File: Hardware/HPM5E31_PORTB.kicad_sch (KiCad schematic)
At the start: 1 part, among them U1 HPM5E31IGN1

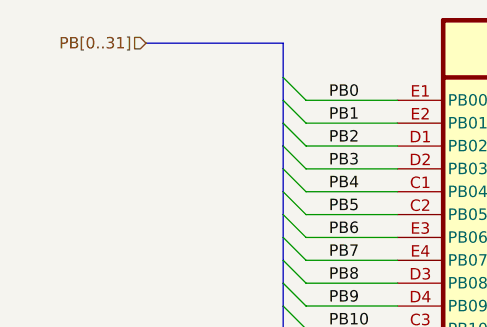
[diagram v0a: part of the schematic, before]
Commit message: 新增ESC IO引出，ESC CTR LED，EUI接口
编码器接口电源输出加保险，SPI加ESD
PY32ADC外部接口加ESD
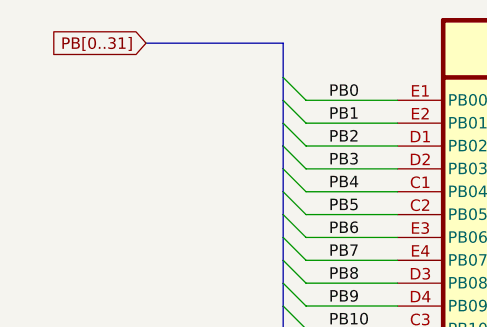
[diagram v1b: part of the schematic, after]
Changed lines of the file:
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@@
 		)
 	)
-	(hierarchical_label "PB[0..31]"
+	(global_label "PB[0..31]"
 		(shape input)
 		(at 58.42 67.31 180)
+		(fields_autoplaced yes)
 		(effects
 			(font
@@
 			(justify right)
 		)
+		(property "Intersheetrefs" "${INTERSHEET_REFS}"
+			(at 46.3633 67.31 0)
+			(effects
+				(font
+					(size 1.27 1.27)
+				)
+				(justify right)
+				(hide yes)
+			)
+		)
 	)

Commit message: 拉线
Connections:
- net PB0: now also U1.M2 (DCDC_IN); no longer U1.E1 (PB00/MCAN0.TXD/ESC0.P0_RXDV/PWM0.P0/TRGM.P00/ETH0.RXDV/QEO1.A)
- net PB1: no longer U1.E2 (PB01/MCAN0.RXD/ESC0.P0_RXD0/PWM0.P1/TRGM.P01/ETH0.RXD0/QEO1.B)
- net PB10: no longer U1.C3 (PB10/MCAN2.STBY/ESC0.P0_TXD3/PWM1.P2/TRGM.P10/ETH0.TXD3)
- net PB11: no longer U1.C4 (PB11/ESC0.P0_TXEN/PWM1.P3/TRGM.P11/ETH0.TXEN)
- net PB2: no longer U1.D1 (PB02/I2C2.SCL/MCAN0.STBY/ESC0.P0_RXD1/PWM0.P2/TRGM.P02/ETH0.RXD1/QEI0.H1/QEO1.Z)
- net PB24: no longer U1.A2 (PB24/ESC0.CTR4/XPI0.CA_CS1/SDM0.CLK3/ETH0.EVTI0/ESC0.EVTI0)
- net PB25: now also U1.J9 (VANA); no longer U1.B1 (PB25/ESC0.CTR5/XPI0.CA_DQS/SDM0.DAT3/ETH0.EVTO0/ESC0.EVTO0)
- net PB26: no longer U1.A3 (PB26/ESC0.CTR6/XPI0.CA_D2/QEI1.H1/SDM0.CLK2/ETH0.EVTI1/EUI1.CK/ESC0.EVTI1)
- net PB27: no longer U1.B2 (PB27/ESC0.CTR7/XPI0.CA_D0/QEI1.F/SDM0.DAT2/EUI1.SH)
- net PB28: now also U1.H8 (VSSA); no longer U1.A4 (PB28/ESC0.CTR8/XPI0.CA_D1/QEI1.H0/SDM0.CLK1/EUI1.DI)
- net PB29: no longer U1.B3 (PB29/XPI0.CA_SCLK/QEI1.Z/SDM0.DAT1/ETH0.EVTO1/EUI1.DO/ESC0.EVTO1)
- net PB3: now also U1.N2 (DCDC_LP); no longer U1.D2 (PB03/I2C2.SDA/MCAN1.STBY/ESC0.P0_RXD2/PWM0.P3/TRGM.P03/ETH0.RXD2/QEI0.F)
- net PB30: no longer U1.A5 (PB30/ESC0.CTR7/XPI0.CA_CS0/QEI1.A/SDM0.CLK0)
- net PB31: no longer U1.B4 (PB31/ESC0.CTR8/XPI0.CA_D3/QEI1.B/SDM0.DAT0)
- net PB4: now also U1.P3 (DCDC_LP); no longer U1.C1 (PB04/MCAN1.RXD/ESC0.P0_RXD3/PWM0.P4/TRGM.P04/ETH0.RXD3/QEI0.H0)
- net PB5: no longer U1.C2 (PB05/MCAN1.TXD/ESC0.P0_RXCK/PWM0.P5/TRGM.P05/ETH0.RXCK/QEI0.Z/QEO0.Z)
- net PB6: no longer U1.E3 (PB06/I2C3.SDA/ESC0.P0_TXCK/PWM0.P6/TRGM.P06/ETH0.TXCK/QEI0.B/QEO0.B)
- net PB7: no longer U1.E4 (PB07/I2C3.SCL/ESC0.P0_TXD0/PWM0.P7/TRGM.P07/ETH0.TXD0/QEI0.A/QEO0.A)
- net PB8: no longer U1.D3 (PB08/I2C0.SCL/MCAN2.TXD/ESC0.P0_TXD1/PWM1.P0/TRGM.P08/ETH0.TXD1)
- net PB9: no longer U1.D4 (PB09/I2C0.SDA/MCAN2.RXD/ESC0.P0_TXD2/PWM1.P1/TRGM.P09/ETH0.TXD2)
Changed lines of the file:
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@@
 		(lib_id "HPM5E00_Library:HPM5E31IGN1")
 		(at 91.44 64.77 0)
-		(unit 5)
+		(unit 1)
 		(exclude_from_sim no)
 		(in_bom yes)
@@
 		(pin "L6"
 		)
-		(instances
-			(project "HPM5E31_ECatDualFOC"
-				(path "/a07e9810-3899-4327-ba8f-f24142a7c70e/b9a8d5a3-7d25-4818-87f6-adc719379948/aa8aabb3-6958-433e-9267-bd903eafdb8f"
-					(reference "U1")
-					(unit 5)
-				)
-			)
-		)
 	)

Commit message: 修存档拉线
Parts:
- renumbered U1 to U3
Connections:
- net PB0: now also U3.E1 (PB00/MCAN0.TXD/ESC0.P0_RXDV/PWM0.P0/TRGM.P00/ETH0.RXDV/QEO1.A); no longer U3.M2 (DCDC_IN)
- net PB1: now also U3.E2 (PB01/MCAN0.RXD/ESC0.P0_RXD0/PWM0.P1/TRGM.P01/ETH0.RXD0/QEO1.B)
- net PB10: now also U3.C3 (PB10/MCAN2.STBY/ESC0.P0_TXD3/PWM1.P2/TRGM.P10/ETH0.TXD3)
- net PB11: now also U3.C4 (PB11/ESC0.P0_TXEN/PWM1.P3/TRGM.P11/ETH0.TXEN)
- net PB2: now also U3.D1 (PB02/I2C2.SCL/MCAN0.STBY/ESC0.P0_RXD1/PWM0.P2/TRGM.P02/ETH0.RXD1/QEI0.H1/QEO1.Z)
- net PB24: now also U3.A2 (PB24/ESC0.CTR4/XPI0.CA_CS1/SDM0.CLK3/ETH0.EVTI0/ESC0.EVTI0)
- net PB25: now also U3.B1 (PB25/ESC0.CTR5/XPI0.CA_DQS/SDM0.DAT3/ETH0.EVTO0/ESC0.EVTO0); no longer U3.J9 (VANA)
- net PB26: now also U3.A3 (PB26/ESC0.CTR6/XPI0.CA_D2/QEI1.H1/SDM0.CLK2/ETH0.EVTI1/EUI1.CK/ESC0.EVTI1)
- net PB27: now also U3.B2 (PB27/ESC0.CTR7/XPI0.CA_D0/QEI1.F/SDM0.DAT2/EUI1.SH)
- net PB28: now also U3.A4 (PB28/ESC0.CTR8/XPI0.CA_D1/QEI1.H0/SDM0.CLK1/EUI1.DI); no longer U3.H8 (VSSA)
- net PB29: now also U3.B3 (PB29/XPI0.CA_SCLK/QEI1.Z/SDM0.DAT1/ETH0.EVTO1/EUI1.DO/ESC0.EVTO1)
- net PB3: now also U3.D2 (PB03/I2C2.SDA/MCAN1.STBY/ESC0.P0_RXD2/PWM0.P3/TRGM.P03/ETH0.RXD2/QEI0.F); no longer U3.N2 (DCDC_LP)
- net PB30: now also U3.A5 (PB30/ESC0.CTR7/XPI0.CA_CS0/QEI1.A/SDM0.CLK0)
- net PB31: now also U3.B4 (PB31/ESC0.CTR8/XPI0.CA_D3/QEI1.B/SDM0.DAT0)
- net PB4: now also U3.C1 (PB04/MCAN1.RXD/ESC0.P0_RXD3/PWM0.P4/TRGM.P04/ETH0.RXD3/QEI0.H0); no longer U3.P3 (DCDC_LP)
- net PB5: now also U3.C2 (PB05/MCAN1.TXD/ESC0.P0_RXCK/PWM0.P5/TRGM.P05/ETH0.RXCK/QEI0.Z/QEO0.Z)
- net PB6: now also U3.E3 (PB06/I2C3.SDA/ESC0.P0_TXCK/PWM0.P6/TRGM.P06/ETH0.TXCK/QEI0.B/QEO0.B)
- net PB7: now also U3.E4 (PB07/I2C3.SCL/ESC0.P0_TXD0/PWM0.P7/TRGM.P07/ETH0.TXD0/QEI0.A/QEO0.A)
- net PB8: now also U3.D3 (PB08/I2C0.SCL/MCAN2.TXD/ESC0.P0_TXD1/PWM1.P0/TRGM.P08/ETH0.TXD1)
- net PB9: now also U3.D4 (PB09/I2C0.SDA/MCAN2.RXD/ESC0.P0_TXD2/PWM1.P1/TRGM.P09/ETH0.TXD2)
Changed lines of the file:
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@@
 		(lib_id "HPM5E00_Library:HPM5E31IGN1")
 		(at 91.44 64.77 0)
-		(unit 1)
+		(unit 5)
 		(exclude_from_sim no)
 		(in_bom yes)
@@
 		(dnp no)
 		(fields_autoplaced yes)
-		(property "Reference" "U1"
+		(property "Reference" "U3"
 			(at 187.96 97.1549 0)
 			(effects
@@
 		(pin "L6"
 		)
+		(instances
+			(project "HPM5E31_ECatDualFOC"
+				(path "/a07e9810-3899-4327-ba8f-f24142a7c70e/b9a8d5a3-7d25-4818-87f6-adc719379948/aa8aabb3-6958-433e-9267-bd903eafdb8f"
+					(reference "U3")
+					(unit 5)
+				)
+			)
+		)
 	)
